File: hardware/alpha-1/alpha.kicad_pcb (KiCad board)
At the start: 2 copper layers, 65 x 56 mm, 82 parts, among them J1 POWER, J2 SERIAL, P1 SWITCH_1, P2 SWITCH_2, P3 SWITCH_3, P4 SWITCH_4, P5 SWITCH_5, P6 SWITCH_6, P7 INPUTS, P8 RASPBERRY_PI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

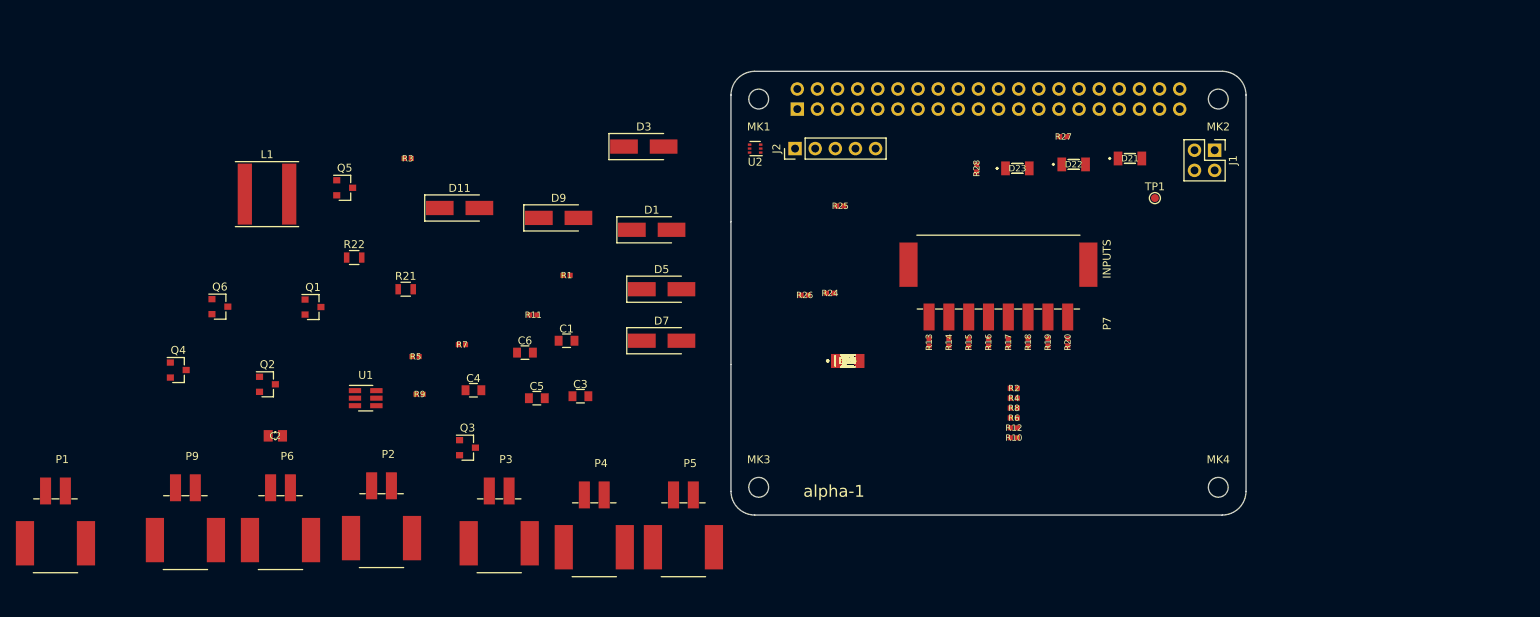
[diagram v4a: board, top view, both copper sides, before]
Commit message: o Updating some footprints, laying out connectors.
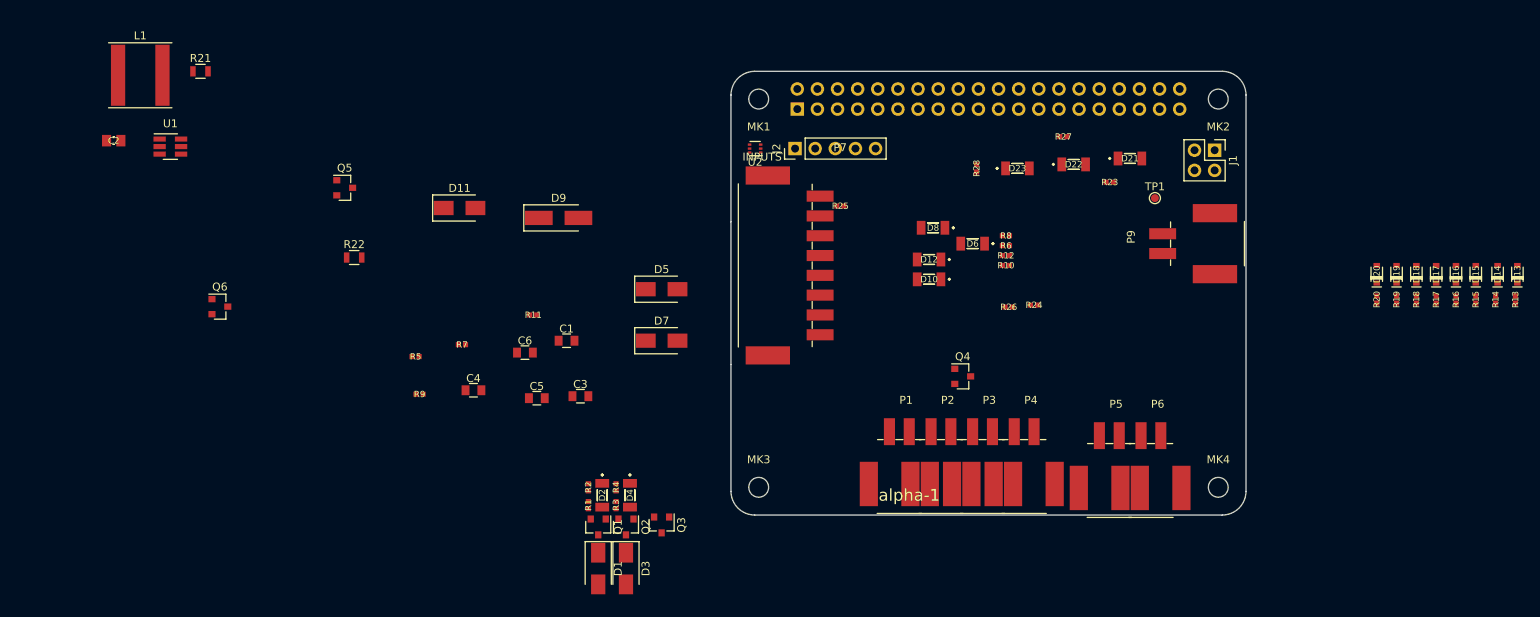
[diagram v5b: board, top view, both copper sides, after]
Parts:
- D1, D11, D3, D5, D7: footprint Diodes_SMD:D_SMA_Handsoldering -> Diodes_SMD:D_SMA
- U2: footprint Bitraf:SOT-553 -> Bitraf:SOT-563
- moved P9 133.3 mm to (259.5, 115.8), turned to 270 degrees
- moved P6 110.0 mm to (253.0, 145.0)
- moved P1 106.8 mm to (221.2, 144.5)
- moved Q4 99.0 mm to (229.2, 132.5)
- moved D13 85.2 mm to (299.2, 119.6), turned to 90 degrees
- moved D14 82.7 mm to (296.8, 119.6), turned to 90 degrees
- moved D15 80.0 mm to (294.0, 119.6), turned to 90 degrees
- moved D16 77.5 mm to (291.5, 119.6), turned to 90 degrees
- moved D17 75.1 mm to (289.0, 119.6), turned to 90 degrees
- moved R13 74.2 mm to (299.0, 122.8), turned to 270 degrees
- moved D18 72.6 mm to (286.5, 119.6), turned to 90 degrees
- moved P2 70.9 mm to (226.5, 144.5)
- moved D19 70.1 mm to (284.0, 119.6), turned to 90 degrees
- moved R14 69.2 mm to (296.5, 122.8), turned to 270 degrees
- moved D20 67.6 mm to (281.5, 119.6), turned to 90 degrees
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
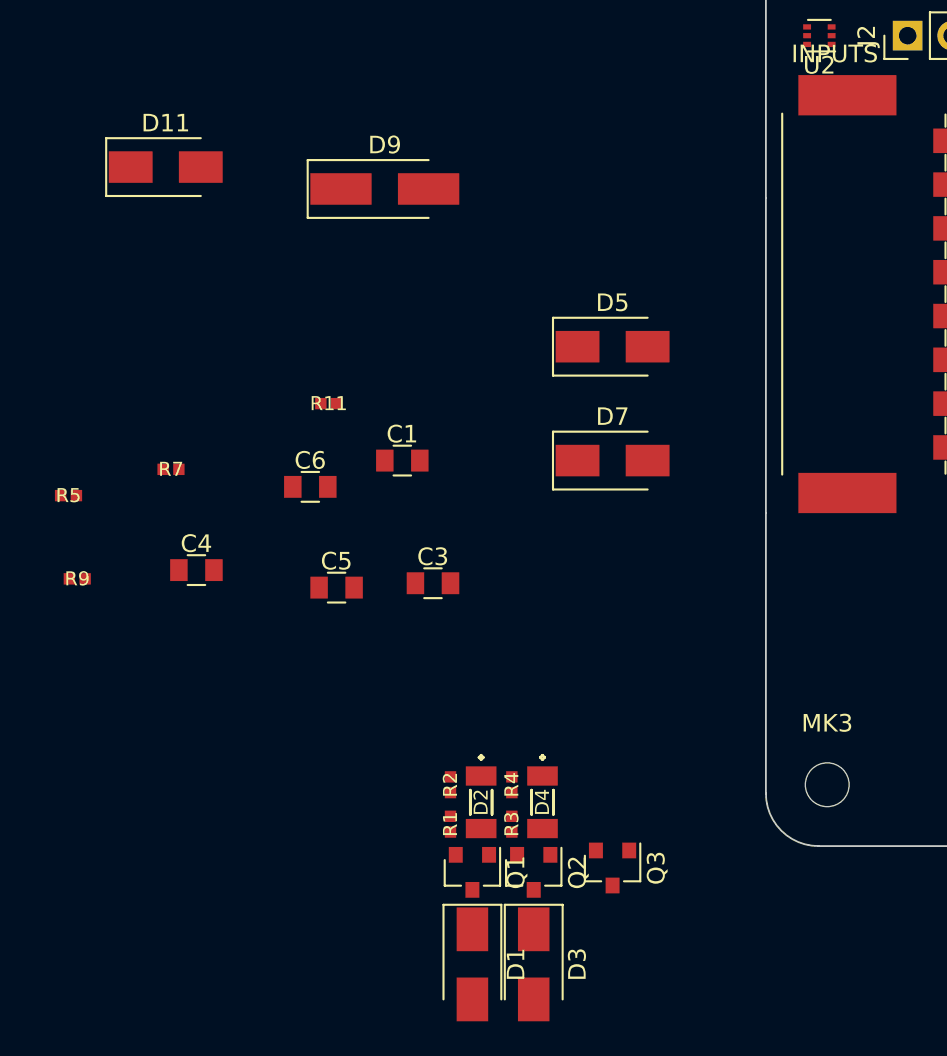
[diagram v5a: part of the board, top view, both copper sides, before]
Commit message: o Adjusting more footprints.
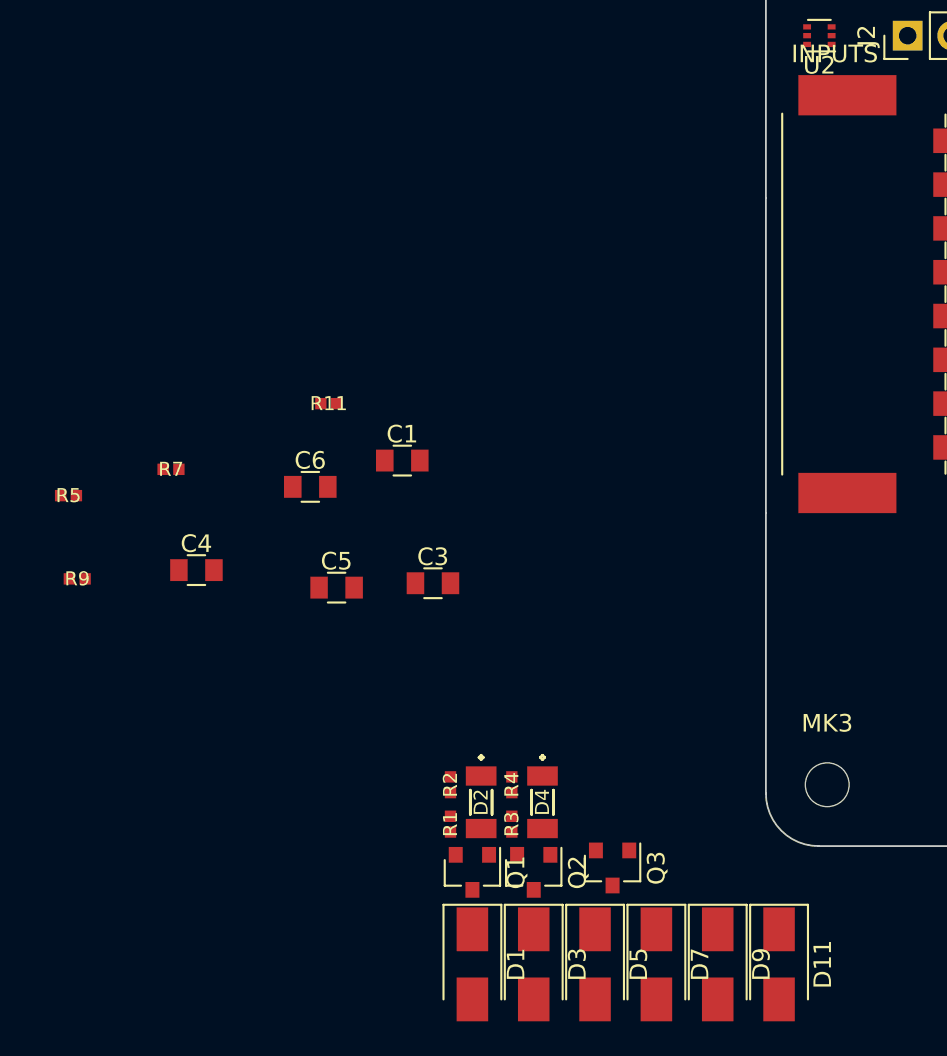
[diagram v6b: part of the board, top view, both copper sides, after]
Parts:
- D9: footprint Diodes_SMD:D_SMA_Handsoldering -> Diodes_SMD:D_SMA
- moved D11 57.4 mm to (200.8, 156.8), turned to 270 degrees
- moved D9 48.2 mm to (197.2, 156.8), turned to 270 degrees
- moved D5 35.3 mm to (190.2, 156.8), turned to 270 degrees
- moved D7 28.9 mm to (193.8, 156.8), turned to 270 degrees
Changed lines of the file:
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@@
-    )
-  )
-  (module Diodes_SMD:D_SMA_Handsoldering (layer F.Cu)
-    (at 178.25 112.5)
-    (descr "Diode SMA (DO-214AC) Handsoldering")
-    (tags "Diode SMA (DO-214AC) Handsoldering")
-    (attr smd)
-    (fp_text reference D9 (at 0 -2.5) (layer F.SilkS)
-      (effects (font (size 1 1) (thickness 0.15)))
-    )
-    (fp_text value S1MTR (at 0 2.6) (layer F.Fab)
-      (effects (font (size 1 1) (thickness 0.15)))
-    )
-    (fp_text user %R (at 0 -2.5) (layer F.Fab)
-      (effects (font (size 1 1) (thickness 0.15)))
-    )
-    (fp_line (start -4.4 -1.65) (end -4.4 1.65) (layer F.SilkS) (width 0.12))
-    (fp_line (start 2.3 1.5) (end -2.3 1.5) (layer F.Fab) (width 0.1))
-    (fp_line (start -2.3 1.5) (end -2.3 -1.5) (layer F.Fab) (width 0.1))
-    (fp_line (start 2.3 -1.5) (end 2.3 1.5) (layer F.Fab) (width 0.1))
-    (fp_line (start 2.3 -1.5) (end -2.3 -1.5) (layer F.Fab) (width 0.1))
-    (fp_line (start -4.5 -1.75) (end 4.5 -1.75) (layer F.CrtYd) (width 0.05))
-    (fp_line (start 4.5 -1.75) (end 4.5 1.75) (layer F.CrtYd) (width 0.05))
-    (fp_line (start 4.5 1.75) (end -4.5 1.75) (layer F.CrtYd) (width 0.05))
-    (fp_line (start -4.5 1.75) (end -4.5 -1.75) (layer F.CrtYd) (width 0.05))
-    (fp_line (start -0.64944 0.00102) (end -1.55114 0.00102) (layer F.Fab) (width 0.1))
-    (fp_line (start 0.50118 0.00102) (end 1.4994 0.00102) (layer F.Fab) (width 0.1))
-    (fp_line (start -0.64944 -0.79908) (end -0.64944 0.80112) (layer F.Fab) (width 0.1))
-    (fp_line (start 0.50118 0.75032) (end 0.50118 -0.79908) (layer F.Fab) (width 0.1))
-    (fp_line (start -0.64944 0.00102) (end 0.50118 0.75032) (layer F.Fab) (width 0.1))
-    (fp_line (start -0.64944 0.00102) (end 0.50118 -0.79908) (layer F.Fab) (width 0.1))
-    (fp_line (start -4.4 1.65) (end 2.5 1.65) (layer F.SilkS) (width 0.12))
-    (fp_line (start -4.4 -1.65) (end 2.5 -1.65) (layer F.SilkS) (width 0.12))
-    (pad 1 smd rect (at -2.5 0) (size 3.5 1.8) (layers F.Cu F.Paste F.Mask)
-      (net 34 Vin))
-    (pad 2 smd rect (at 2.5 0) (size 3.5 1.8) (layers F.Cu F.Paste F.Mask)
-      (net 40 "Net-(D9-Pad2)"))
-    (model ${KISYS3DMOD}/Diodes_SMD.3dshapes/D_SMA.wrl
-      (at (xyz 0 0 0))
-      (scale (xyz 1 1 1))
-      (rotate (xyz 0 0 0))
     )
   )
@@
   )
   (module Diodes_SMD:D_SMA (layer F.Cu)
-    (at 191.25 121.5)
+    (at 190.25 156.75 270)
     (descr "Diode SMA (DO-214AC)")
     (tags "Diode SMA (DO-214AC)")
     (attr smd)
-    (fp_text reference D5 (at 0 -2.5) (layer F.SilkS)
-      (effects (font (size 1 1) (thickness 0.15)))
-    )
-    (fp_text value S1MTR (at 0 2.6) (layer F.Fab)
-      (effects (font (size 1 1) (thickness 0.15)))
-    )
-    (fp_text user %R (at 0 -2.5) (layer F.Fab)
+    (fp_text reference D5 (at 0 -2.5 270) (layer F.SilkS)
+      (effects (font (size 1 1) (thickness 0.15)))
+    )
+    (fp_text value S1MTR (at 0 2.6 270) (layer F.Fab)
+      (effects (font (size 1 1) (thickness 0.15)))
+    )
+    (fp_text user %R (at 0 -2.5 270) (layer F.Fab)
       (effects (font (size 1 1) (thickness 0.15)))
     )
@@
     (fp_line (start -3.4 1.65) (end 2 1.65) (layer F.SilkS) (width 0.12))
     (fp_line (start -3.4 -1.65) (end 2 -1.65) (layer F.SilkS) (width 0.12))
-    (pad 1 smd rect (at -2 0) (size 2.5 1.8) (layers F.Cu F.Paste F.Mask)
+    (pad 1 smd rect (at -2 0 270) (size 2.5 1.8) (layers F.Cu F.Paste F.Mask)
       (net 34 Vin))
-    (pad 2 smd rect (at 2 0) (size 2.5 1.8) (layers F.Cu F.Paste F.Mask)
+    (pad 2 smd rect (at 2 0 270) (size 2.5 1.8) (layers F.Cu F.Paste F.Mask)
       (net 38 "Net-(D5-Pad2)"))
     (model ${KISYS3DMOD}/Diodes_SMD.3dshapes/D_SMA.wrl
@@
   )
   (module Diodes_SMD:D_SMA (layer F.Cu)
-    (at 191.25 128)
+    (at 193.75 156.75 270)
     (descr "Diode SMA (DO-214AC)")
     (tags "Diode SMA (DO-214AC)")
     (attr smd)
-    (fp_text reference D7 (at 0 -2.5) (layer F.SilkS)
-      (effects (font (size 1 1) (thickness 0.15)))
-    )
-    (fp_text value S1MTR (at 0 2.6) (layer F.Fab)
-      (effects (font (size 1 1) (thickness 0.15)))
-    )
-    (fp_text user %R (at 0 -2.5) (layer F.Fab)
+    (fp_text reference D7 (at 0 -2.5 270) (layer F.SilkS)
+      (effects (font (size 1 1) (thickness 0.15)))
+    )
+    (fp_text value S1MTR (at 0 2.6 270) (layer F.Fab)
+      (effects (font (size 1 1) (thickness 0.15)))
+    )
+    (fp_text user %R (at 0 -2.5 270) (layer F.Fab)
       (effects (font (size 1 1) (thickness 0.15)))
     )
@@
     (fp_line (start -3.4 1.65) (end 2 1.65) (layer F.SilkS) (width 0.12))
     (fp_line (start -3.4 -1.65) (end 2 -1.65) (layer F.SilkS) (width 0.12))
-    (pad 1 smd rect (at -2 0) (size 2.5 1.8) (layers F.Cu F.Paste F.Mask)
+    (pad 1 smd rect (at -2 0 270) (size 2.5 1.8) (layers F.Cu F.Paste F.Mask)
       (net 34 Vin))
-    (pad 2 smd rect (at 2 0) (size 2.5 1.8) (layers F.Cu F.Paste F.Mask)
+    (pad 2 smd rect (at 2 0 270) (size 2.5 1.8) (layers F.Cu F.Paste F.Mask)
       (net 39 "Net-(D7-Pad2)"))
     (model ${KISYS3DMOD}/Diodes_SMD.3dshapes/D_SMA.wrl
@@
   )
   (module Diodes_SMD:D_SMA (layer F.Cu)
-    (at 165.75 111.25)
+    (at 200.75 156.75 270)
     (descr "Diode SMA (DO-214AC)")
     (tags "Diode SMA (DO-214AC)")
     (attr smd)
-    (fp_text reference D11 (at 0 -2.5) (layer F.SilkS)
-      (effects (font (size 1 1) (thickness 0.15)))
-    )
-    (fp_text value S1MTR (at 0 2.6) (layer F.Fab)
-      (effects (font (size 1 1) (thickness 0.15)))
-    )
-    (fp_text user %R (at 0 -2.5) (layer F.Fab)
+    (fp_text reference D11 (at 0 -2.5 270) (layer F.SilkS)
+      (effects (font (size 1 1) (thickness 0.15)))
+    )
+    (fp_text value S1MTR (at 0 2.6 270) (layer F.Fab)
+      (effects (font (size 1 1) (thickness 0.15)))
+    )
+    (fp_text user %R (at 0 -2.5 270) (layer F.Fab)
       (effects (font (size 1 1) (thickness 0.15)))
     )
@@
     (fp_line (start -3.4 1.65) (end 2 1.65) (layer F.SilkS) (width 0.12))
     (fp_line (start -3.4 -1.65) (end 2 -1.65) (layer F.SilkS) (width 0.12))
-    (pad 1 smd rect (at -2 0) (size 2.5 1.8) (layers F.Cu F.Paste F.Mask)
+    (pad 1 smd rect (at -2 0 270) (size 2.5 1.8) (layers F.Cu F.Paste F.Mask)
       (net 34 Vin))
-    (pad 2 smd rect (at 2 0) (size 2.5 1.8) (layers F.Cu F.Paste F.Mask)
+    (pad 2 smd rect (at 2 0 270) (size 2.5 1.8) (layers F.Cu F.Paste F.Mask)
       (net 41 "Net-(D11-Pad2)"))
     (model ${KISYS3DMOD}/Diodes_SMD.3dshapes/D_SMA.wrl
       (at (xyz 0 0 0))
+      (scale (xyz 1 1 1))
+      (rotate (xyz 0 0 0))
+    )
+  )
+  (module Diodes_SMD:D_SMA (layer F.Cu)
+    (at 197.25 156.75 270)
+    (descr "Diode SMA (DO-214AC)")
+    (tags "Diode SMA (DO-214AC)")
+    (attr smd)
+    (fp_text reference D9 (at 0 -2.5 270) (layer F.SilkS)
+      (effects (font (size 1 1) (thickness 0.15)))
+    )
+    (fp_text value S1MTR (at 0 2.6 270) (layer F.Fab)
+      (effects (font (size 1 1) (thickness 0.15)))
+    )
+    (fp_text user %R (at 0 -2.5 270) (layer F.Fab)
+      (effects (font (size 1 1) (thickness 0.15)))
+    )
+    (fp_line (start -3.4 -1.65) (end -3.4 1.65) (layer F.SilkS) (width 0.12))
+    (fp_line (start 2.3 1.5) (end -2.3 1.5) (layer F.Fab) (width 0.1))
+    (fp_line (start -2.3 1.5) (end -2.3 -1.5) (layer F.Fab) (width 0.1))
+    (fp_line (start 2.3 -1.5) (end 2.3 1.5) (layer F.Fab) (width 0.1))
+    (fp_line (start 2.3 -1.5) (end -2.3 -1.5) (layer F.Fab) (width 0.1))
+    (fp_line (start -3.5 -1.75) (end 3.5 -1.75) (layer F.CrtYd) (width 0.05))
+    (fp_line (start 3.5 -1.75) (end 3.5 1.75) (layer F.CrtYd) (width 0.05))
+    (fp_line (start 3.5 1.75) (end -3.5 1.75) (layer F.CrtYd) (width 0.05))
+    (fp_line (start -3.5 1.75) (end -3.5 -1.75) (layer F.CrtYd) (width 0.05))
+    (fp_line (start -0.64944 0.00102) (end -1.55114 0.00102) (layer F.Fab) (width 0.1))
+    (fp_line (start 0.50118 0.00102) (end 1.4994 0.00102) (layer F.Fab) (width 0.1))
+    (fp_line (start -0.64944 -0.79908) (end -0.64944 0.80112) (layer F.Fab) (width 0.1))
+    (fp_line (start 0.50118 0.75032) (end 0.50118 -0.79908) (layer F.Fab) (width 0.1))
+    (fp_line (start -0.64944 0.00102) (end 0.50118 0.75032) (layer F.Fab) (width 0.1))
+    (fp_line (start -0.64944 0.00102) (end 0.50118 -0.79908) (layer F.Fab) (width 0.1))
+    (fp_line (start -3.4 1.65) (end 2 1.65) (layer F.SilkS) (width 0.12))
+    (fp_line (start -3.4 -1.65) (end 2 -1.65) (layer F.SilkS) (width 0.12))
+    (pad 1 smd rect (at -2 0 270) (size 2.5 1.8) (layers F.Cu F.Paste F.Mask)
+      (net 34 Vin))
+    (pad 2 smd rect (at 2 0 270) (size 2.5 1.8) (layers F.Cu F.Paste F.Mask)
+      (net 40 "Net-(D9-Pad2)"))
+    (model ${KISYS3DMOD}/Diodes_SMD.3dshapes/D_SMA.wrl
+      (at (xyz 0 0 0))
